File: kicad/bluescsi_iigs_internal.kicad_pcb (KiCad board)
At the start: 2 copper layers, 61.5 x 55.4 mm, 27 parts, among them J1 Conn_02x13_Odd_Even, J2 Conn_02x13_Odd_Even, J3 105162-0001, J4 Conn_01x02_Male, J5 Conn_01x02_Male, J6 DB25_Male, M1 Screw_Terminal_01x01, M2 Screw_Terminal_01x01, SW1 SW_SPDT, U1 YAAJ_BluePill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

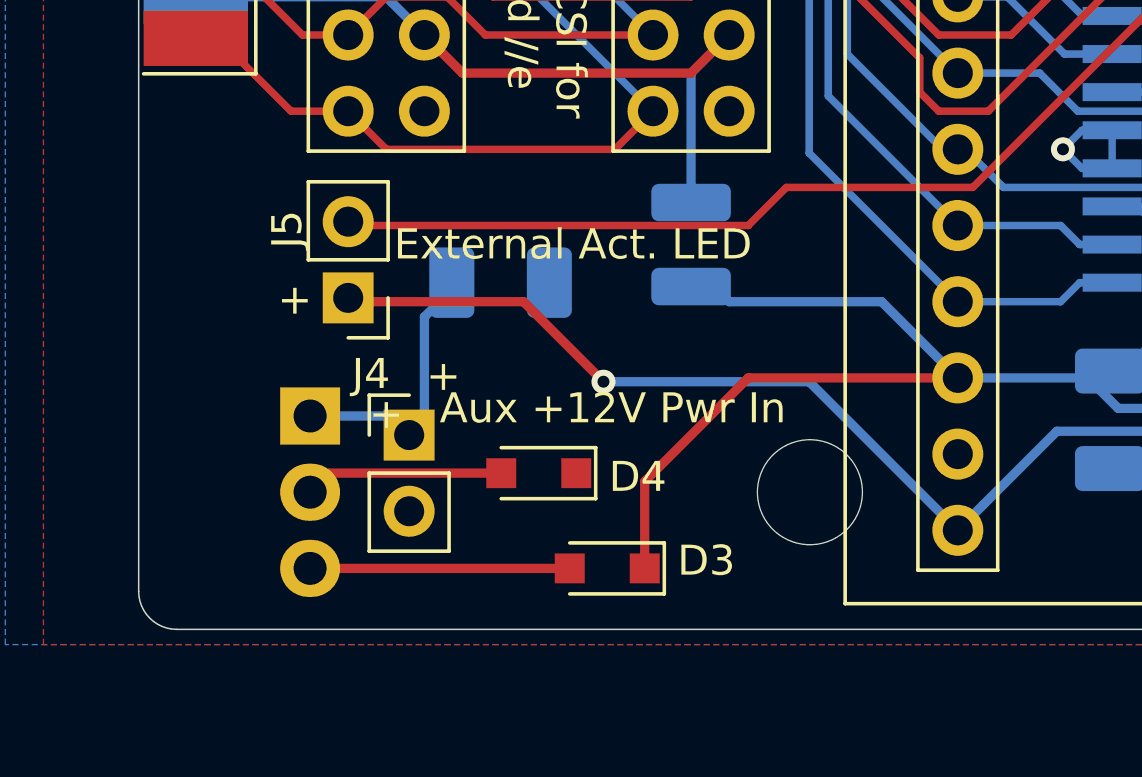
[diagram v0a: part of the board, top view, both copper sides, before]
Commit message: move the regulator around so the screw hole doesn't overlap the blue pill footprint
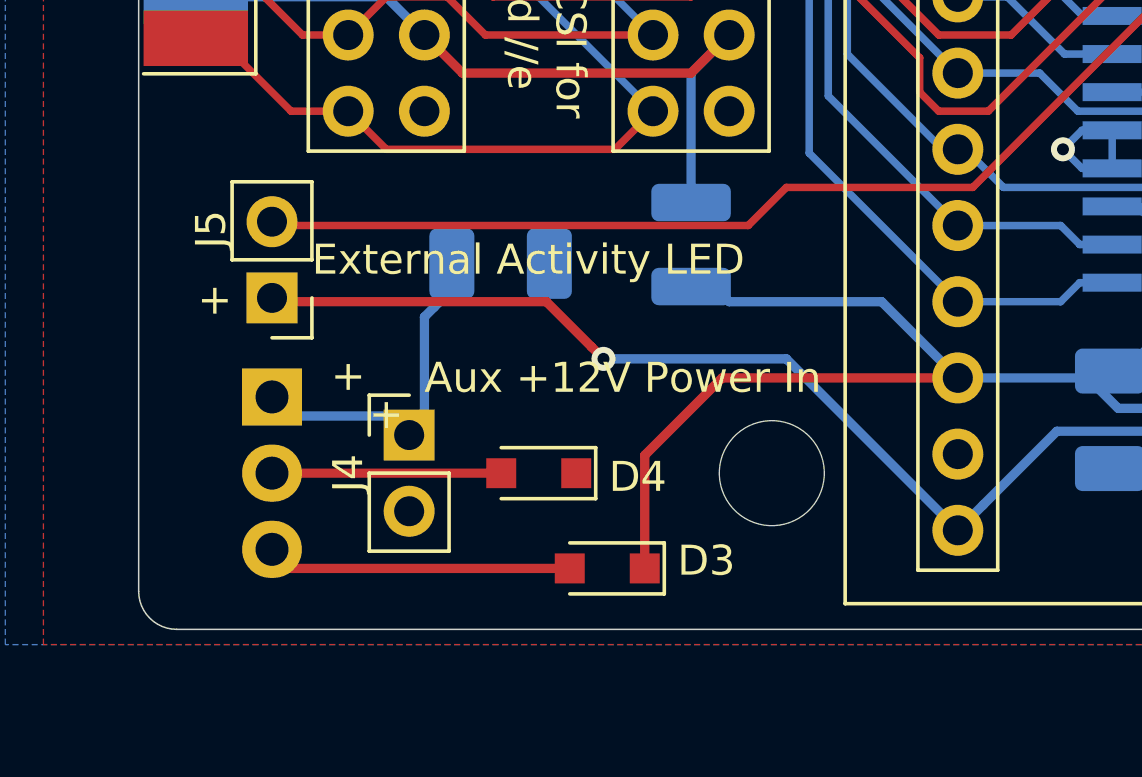
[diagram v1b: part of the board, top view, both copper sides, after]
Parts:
- moved J5 2.54 mm to (129.5, 91.3)
- moved U4 1.42 mm to (129.5, 94.6)
- moved C4 0.64 mm to (137.2, 90.2)
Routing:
- net Net-(D1-Pad1): track 62.7 -> 65.9 mm
- net +3V3: track 101.4 -> 104.0 mm
- net /REG_OUT: track 8.66 -> 10.2 mm
- net /+12V_AUX: track 9.27 -> 10.5 mm
- net Net-(D4-Pad2): track 6.63 -> 7.64 mm
- net +5V: track 112.7 -> 113.2 mm
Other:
- board text added: "Aux +12V Power In"
- board text added: "External Activity LED"
- board text removed: "Aux +12V Pwr In"
- board text removed: "External Act. LED"
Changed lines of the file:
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@@
     (thickness 1.6)
     (drawings 59)
-    (tracks 574)
+    (tracks 579)
     (zones 0)
     (modules 27)
@@
   )
   (module Package_TO_SOT_THT:TO-220-3_Horizontal_TabUp (layer B.Cu)
-    (at 130.81 95.25 270)
+    (at 129.54 94.615 270)
     (descr "TO-220-3, Horizontal, RM 2.54mm, see https://www.vishay.com/docs/66542/to-220-1.pdf")
     (tags "TO-220-3 Horizontal RM 2.54mm")
@@
   )
   (module Connector_PinHeader_2.54mm:PinHeader_1x02_P2.54mm_Vertical (layer F.Cu)
-    (at 132.08 91.313 180)
+    (at 129.54 91.313 180)
     (descr "Through hole straight pin header, 1x02, 2.54mm pitch, single row")
     (tags "Through hole pin header THT 1x02 2.54mm single row")
@@
     (descr "Through hole straight pin header, 1x02, 2.54mm pitch, single row")
     (tags "Through hole pin header THT 1x02 2.54mm single row")
-    (fp_text reference J4 (at -1.27 -2.032 180) (layer F.SilkS)
+    (fp_text reference J4 (at -2.032 1.27 270) (layer F.SilkS)
       (effects (font (size 1 1) (thickness 0.15)))
     )
@@
   )
   (module Capacitor_Tantalum_SMD:CP_EIA-3528-21_Kemet-B_Pad1.50x2.35mm_HandSolder (layer B.Cu)
-    (at 137.16 90.805)
+    (at 137.16 90.17)
     (descr "Tantalum Capacitor SMD Kemet-B (3528-21 Metric), IPC_7351 nominal, (Body size from: http://www.kemet.com/Lists/ProductCatalog/Attachments/253/KEM_TC101_STD.pdf), generated with kicad-footprint-generator")
     (tags "capacitor tantalum")
@@
     (effects (font (size 1 1) (thickness 0.15)) (justify mirror))
   )
-  (gr_text "External Act. LED" (at 133.604 89.535) (layer F.SilkS)
+  (gr_text "External Activity LED" (at 130.87 90.043) (layer F.SilkS)
     (effects (font (size 1 1) (thickness 0.15)) (justify left))
   )
-  (gr_text + (at 130.302 91.44 180) (layer F.SilkS)
+  (gr_text + (at 127.635 91.44 180) (layer F.SilkS)
     (effects (font (size 1 1) (thickness 0.15)))
   )
@@
     (effects (font (size 1 1) (thickness 0.15)))
   )
-  (gr_text + (at 135.255 93.98 180) (layer F.SilkS)
+  (gr_text + (at 132.08 93.98 180) (layer F.SilkS)
     (effects (font (size 1 1) (thickness 0.15)))
   )
-  (gr_text "Aux +12V Pwr In" (at 135.128 94.996) (layer F.SilkS)
+  (gr_text "Aux +12V Power In" (at 134.62 93.98) (layer F.SilkS)
     (effects (font (size 1 1) (thickness 0.15)) (justify left))
   )
@@
   (segment (start 173.833 66.421) (end 173.579 66.675) (width 0.31) (layer F.Cu) (net 12))
   (via (at 170.814998 66.675) (size 0.8) (drill 0.4) (layers F.Cu B.Cu) (net 12))
-  (segment (start 145.415 93.98) (end 152.4 93.98) (width 0.31) (layer F.Cu) (net 12))
-  (segment (start 141.966 97.429) (end 145.415 93.98) (width 0.31) (layer F.Cu) (net 12))
-  (segment (start 141.966 100.33) (end 141.966 97.429) (width 0.31) (layer F.Cu) (net 12))
   (segment (start 174.498 89.408) (end 170.307 85.217) (width 0.31) (layer F.Cu) (net 12))
   (segment (start 176.927 89.408) (end 174.498 89.408) (width 0.31) (layer F.Cu) (net 12))
@@
   (segment (start 144.145 90.805) (end 144.78 91.44) (width 0.31) (layer B.Cu) (net 12))
   (segment (start 143.51 90.805) (end 144.145 90.805) (width 0.31) (layer B.Cu) (net 12))
+  (segment (start 141.966 100.33) (end 141.966 96.555875) (width 0.31) (layer F.Cu) (net 12))
+  (segment (start 141.966 96.555875) (end 144.541875 93.98) (width 0.31) (layer F.Cu) (net 12))
+  (segment (start 144.541875 93.98) (end 152.4 93.98) (width 0.31) (layer F.Cu) (net 12))
   (segment (start 157.545 85.725) (end 157.545 86.995) (width 0.25) (layer B.Cu) (net 13) (status 30))
   (segment (start 157.545 60.325) (end 162.495 60.325) (width 0.25) (layer B.Cu) (net 13) (status 30))
@@
   (segment (start 173.228 85.725) (end 171.45 83.947) (width 0.31) (layer F.Cu) (net 34))
   (segment (start 176.927 85.725) (end 173.228 85.725) (width 0.31) (layer F.Cu) (net 34))
-  (segment (start 147.447 94.107) (end 140.589 94.107) (width 0.31) (layer B.Cu) (net 34))
-  (segment (start 132.08 91.44) (end 137.922 91.44) (width 0.31) (layer F.Cu) (net 34))
-  (segment (start 137.922 91.44) (end 140.589 94.107) (width 0.31) (layer F.Cu) (net 34))
-  (segment (start 152.4 99.06) (end 147.447 94.107) (width 0.31) (layer B.Cu) (net 34))
-  (via (at 140.589 94.107) (size 0.8) (drill 0.4) (layers F.Cu B.Cu) (net 34))
   (segment (start 172.357999 75.075999) (end 170.561 73.279) (width 0.31) (layer F.Cu) (net 34))
   (segment (start 181.823001 75.075999) (end 172.357999 75.075999) (width 0.31) (layer F.Cu) (net 34))
   (segment (start 181.965 74.934) (end 181.823001 75.075999) (width 0.31) (layer F.Cu) (net 34))
+  (segment (start 152.4 99.06) (end 146.685 93.345) (width 0.31) (layer B.Cu) (net 34))
+  (segment (start 146.685 93.345) (end 140.589 93.345) (width 0.31) (layer B.Cu) (net 34))
+  (via (at 140.589 93.345) (size 0.8) (drill 0.4) (layers F.Cu B.Cu) (net 34))
+  (segment (start 138.684 91.44) (end 140.189001 92.945001) (width 0.31) (layer F.Cu) (net 34))
+  (segment (start 129.667 91.44) (end 138.684 91.44) (width 0.31) (layer F.Cu) (net 34))
+  (segment (start 140.189001 92.945001) (end 140.589 93.345) (width 0.31) (layer F.Cu) (net 34))
+  (segment (start 129.54 91.313) (end 129.667 91.44) (width 0.31) (layer F.Cu) (net 34))
   (segment (start 181.918 73.787) (end 181.965 73.834) (width 0.25) (layer F.Cu) (net 35))
   (segment (start 180.721 73.787) (end 181.918 73.787) (width 0.25) (layer F.Cu) (net 35))
@@
   (segment (start 172.856 83.811) (end 172.847 83.82) (width 0.25) (layer F.Cu) (net 43))
   (segment (start 184.531 83.811) (end 172.856 83.811) (width 0.25) (layer F.Cu) (net 43))
-  (segment (start 169.037 80.01) (end 172.847 83.82) (width 0.25) (layer F.Cu) (net 43))
-  (segment (start 146.685 87.63) (end 152.898251 87.63) (width 0.25) (layer F.Cu) (net 43))
-  (segment (start 132.715 88.9) (end 145.415 88.9) (width 0.25) (layer F.Cu) (net 43))
-  (segment (start 152.898251 87.63) (end 160.518251 80.01) (width 0.25) (layer F.Cu) (net 43))
-  (segment (start 160.518251 80.01) (end 169.037 80.01) (width 0.25) (layer F.Cu) (net 43))
-  (segment (start 145.415 88.9) (end 146.685 87.63) (width 0.25) (layer F.Cu) (net 43))
   (segment (start 172.847 84.385685) (end 172.847 83.82) (width 0.25) (layer B.Cu) (net 43))
   (segment (start 172.847 87.754) (end 172.847 84.385685) (width 0.25) (layer B.Cu) (net 43))
   (segment (start 172.067 88.534) (end 172.847 87.754) (width 0.25) (layer B.Cu) (net 43))
   (segment (start 171.517 88.534) (end 172.067 88.534) (width 0.25) (layer B.Cu) (net 43))
-  (segment (start 131.445 97.155) (end 130.81 97.79) (width 0.31) (layer B.Cu) (net 46))
-  (segment (start 137.18 97.155) (end 131.445 97.155) (width 0.31) (layer F.Cu) (net 46))
-  (segment (start 130.81 95.25) (end 133.985 95.25) (width 0.31) (layer B.Cu) (net 47))
-  (segment (start 134.62 95.885) (end 134.62 91.948) (width 0.31) (layer B.Cu) (net 47))
+  (segment (start 169.037 80.01) (end 172.847 83.82) (width 0.25) (layer F.Cu) (net 43))
+  (segment (start 152.898251 87.63) (end 160.518251 80.01) (width 0.25) (layer F.Cu) (net 43))
+  (segment (start 129.54 88.773) (end 129.667 88.9) (width 0.25) (layer F.Cu) (net 43))
+  (segment (start 146.685 87.63) (end 152.898251 87.63) (width 0.25) (layer F.Cu) (net 43))
+  (segment (start 160.518251 80.01) (end 169.037 80.01) (width 0.25) (layer F.Cu) (net 43))
+  (segment (start 129.667 88.9) (end 145.415 88.9) (width 0.25) (layer F.Cu) (net 43))
+  (segment (start 145.415 88.9) (end 146.685 87.63) (width 0.25) (layer F.Cu) (net 43))
+  (segment (start 137.18 97.155) (end 129.54 97.155) (width 0.31) (layer F.Cu) (net 46))
+  (segment (start 134.9375 91.6305) (end 135.509 91.059) (width 0.31) (layer B.Cu) (net 47))
   (segment (start 134.62 91.948) (end 134.9375 91.6305) (width 0.31) (layer B.Cu) (net 47))
-  (segment (start 134.9375 91.6305) (end 135.509 91.059) (width 0.31) (layer B.Cu) (net 47))
-  (segment (start 133.985 95.25) (end 134.62 95.885) (width 0.31) (layer B.Cu) (net 47))
+  (segment (start 130.175 95.25) (end 133.477 95.25) (width 0.31) (layer B.Cu) (net 47))
+  (segment (start 134.62 95.377) (end 134.62 91.948) (width 0.31) (layer B.Cu) (net 47))
+  (segment (start 133.477 95.25) (end 134.112 95.885) (width 0.31) (layer B.Cu) (net 47))
+  (segment (start 134.112 95.885) (end 134.62 95.377) (width 0.31) (layer B.Cu) (net 47))
+  (segment (start 129.54 94.615) (end 130.175 95.25) (width 0.31) (layer B.Cu) (net 47))
   (segment (start 175.133 62.23) (end 175.26 62.23) (width 0.25) (layer F.Cu) (net 48))
   (segment (start 175.776201 62.797001) (end 177.774998 62.797001) (width 0.25) (layer F.Cu) (net 48))
@@
   (segment (start 173.355 87.884) (end 173.101 88.138) (width 0.25) (layer B.Cu) (net 50))
   (segment (start 174.177 87.884) (end 173.355 87.884) (width 0.25) (layer B.Cu) (net 50))
-  (segment (start 130.81 100.33) (end 139.466 100.33) (width 0.31) (layer F.Cu) (net 51))
+  (segment (start 130.175 100.33) (end 139.466 100.33) (width 0.31) (layer F.Cu) (net 51))
+  (segment (start 129.54 99.695) (end 130.175 100.33) (width 0.31) (layer F.Cu) (net 51))
   (segment (start 143.51 83.82) (end 144.78 82.55) (width 0.31) (layer F.Cu) (net 52))
   (segment (start 135.89 83.82) (end 143.51 83.82) (width 0.31) (layer F.Cu) (net 52))
